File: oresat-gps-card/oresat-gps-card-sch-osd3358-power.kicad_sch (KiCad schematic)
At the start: 52 parts, among them Q6 MMBT2907, U1 OSD3358-512M-BSM, U10 SN74LVC1G07DCK, U13 RCLAMP0504FB, U14 TLVH431

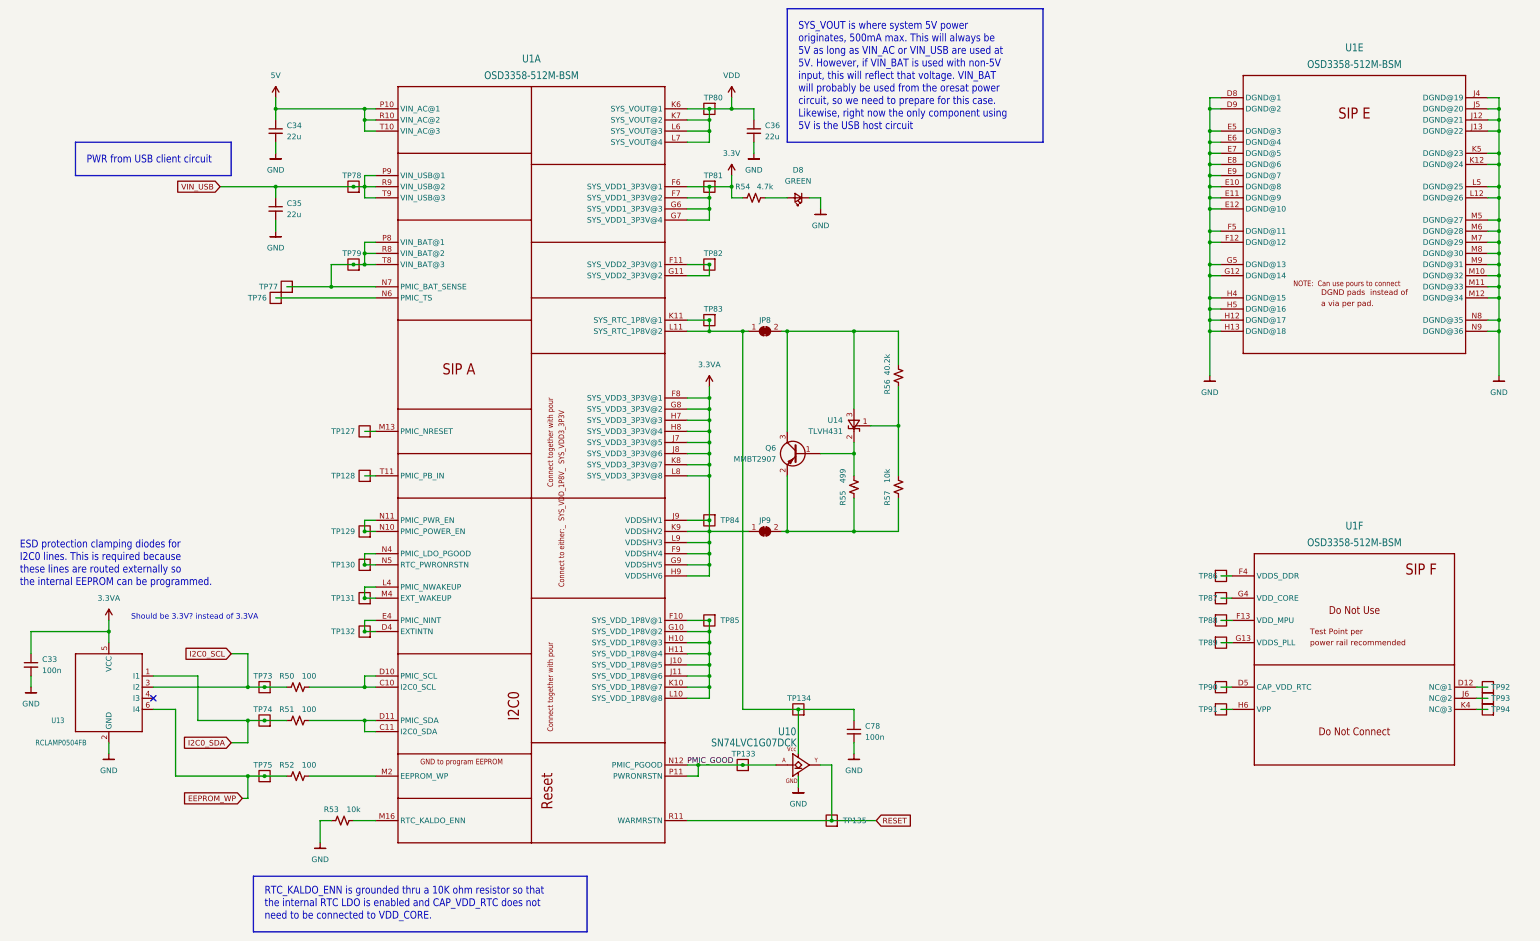
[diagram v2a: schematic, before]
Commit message: Updated GPS card with changes from C3 and notes. Fixed library issues
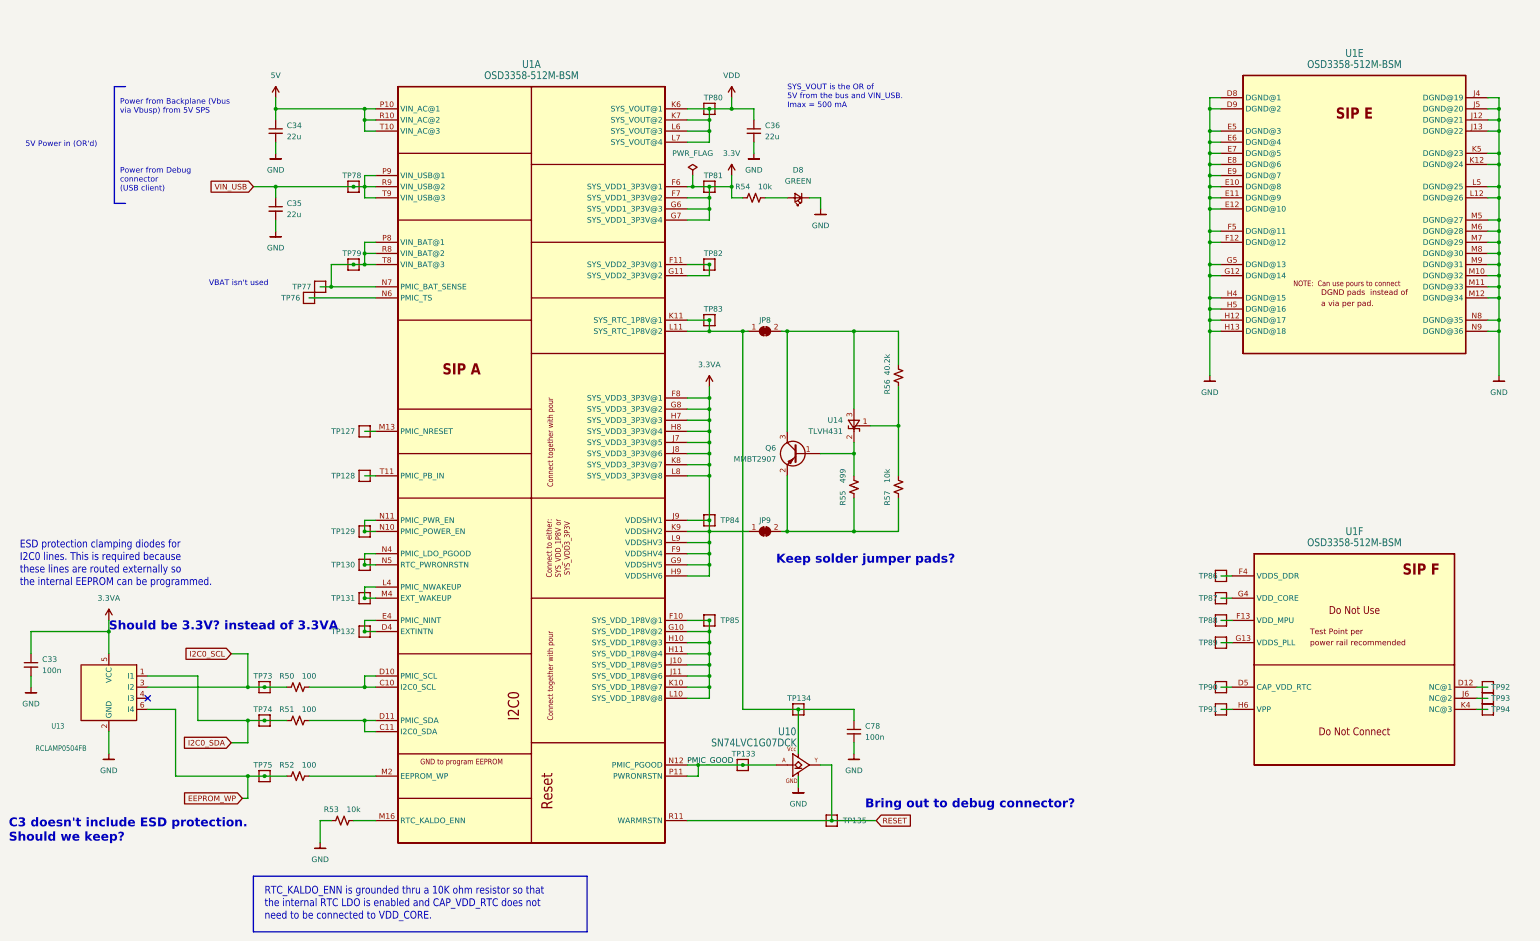
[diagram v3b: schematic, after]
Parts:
- R54: value 4.7k -> 10k
- TP127, TP128, TP129, TP130, TP131, TP132, TP133, TP134, TP135, TP73, TP74, TP75, TP76, TP77, TP78, TP79, TP80, TP81, TP82, TP83, TP84, TP85, TP86, TP87, TP88, TP89, TP90, TP91, TP92, TP93, TP94: value Test-Point -> 0.03x0.04; footprint OreSat-TestPoint:PAD.03X.04 -> oresat-misc:TestPoint_Pad_D1.0mm; symbol OreSat-TestPoint:Test-Point -> oresat-misc:Test-Point-1mm-round
- U1: footprint oresat-footprints:U-Octavo-OSD335X-BGA-256 -> oresat-ics:U-Octavo-OSD335X-BGA-256; symbol U-OSD3358-512M-BSM:OSD3358-512M-BSM -> oresat-ics:OSD3358-512M-BSM
- U10: symbol U-TI-SN74LVC1G07DCK:SN74LVC1G07DCK -> oresat-ics:SN74LVC1G07DCK
- U13: symbol U-Semtech-RCLAMP0504FB-tvs-diodes:RCLAMP0504FB -> oresat-ics:RCLAMP0504FB
- U14: footprint oresat-footprints:SOT23 -> Package_TO_SOT_SMD:SOT-23; symbol U-TI-TLVH431-shunt-regulator:TLVH431 -> oresat-ics:TLVH431
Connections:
- net VDD renamed 1.1V
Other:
- note added: "5V Power in (OR'd)"
- note added: "Bring out to debug connector?"
- note added: "C3 doesn't include ESD protection. Should we keep?"
- note added: "Keep solder jumper pads?"
- note added: "Power from Backplane (Vbus via Vbusp) from 5V SPS"
- note added: "Power from Debug connector (USB client)"
- note added: "SYS_VOUT is the OR of 5V from the bus and VIN_USB. Imax = 500 mA"
- note added: "VBAT isn't used"
- note removed: "PWR from USB client circuit"
- note removed: "SYS_VOUT is where system 5V power originates, 500mA max. This will always be 5V as long as VIN_AC or VIN_USB are used at 5V. However, if VIN_BAT is used with non-5V input, this will reflect that voltage. VIN_BAT will probably be used from the oresat power circuit, so we need to prepare for this case. Likewise, right now the only component using 5V is the USB host circuit"

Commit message: Updated GPS card
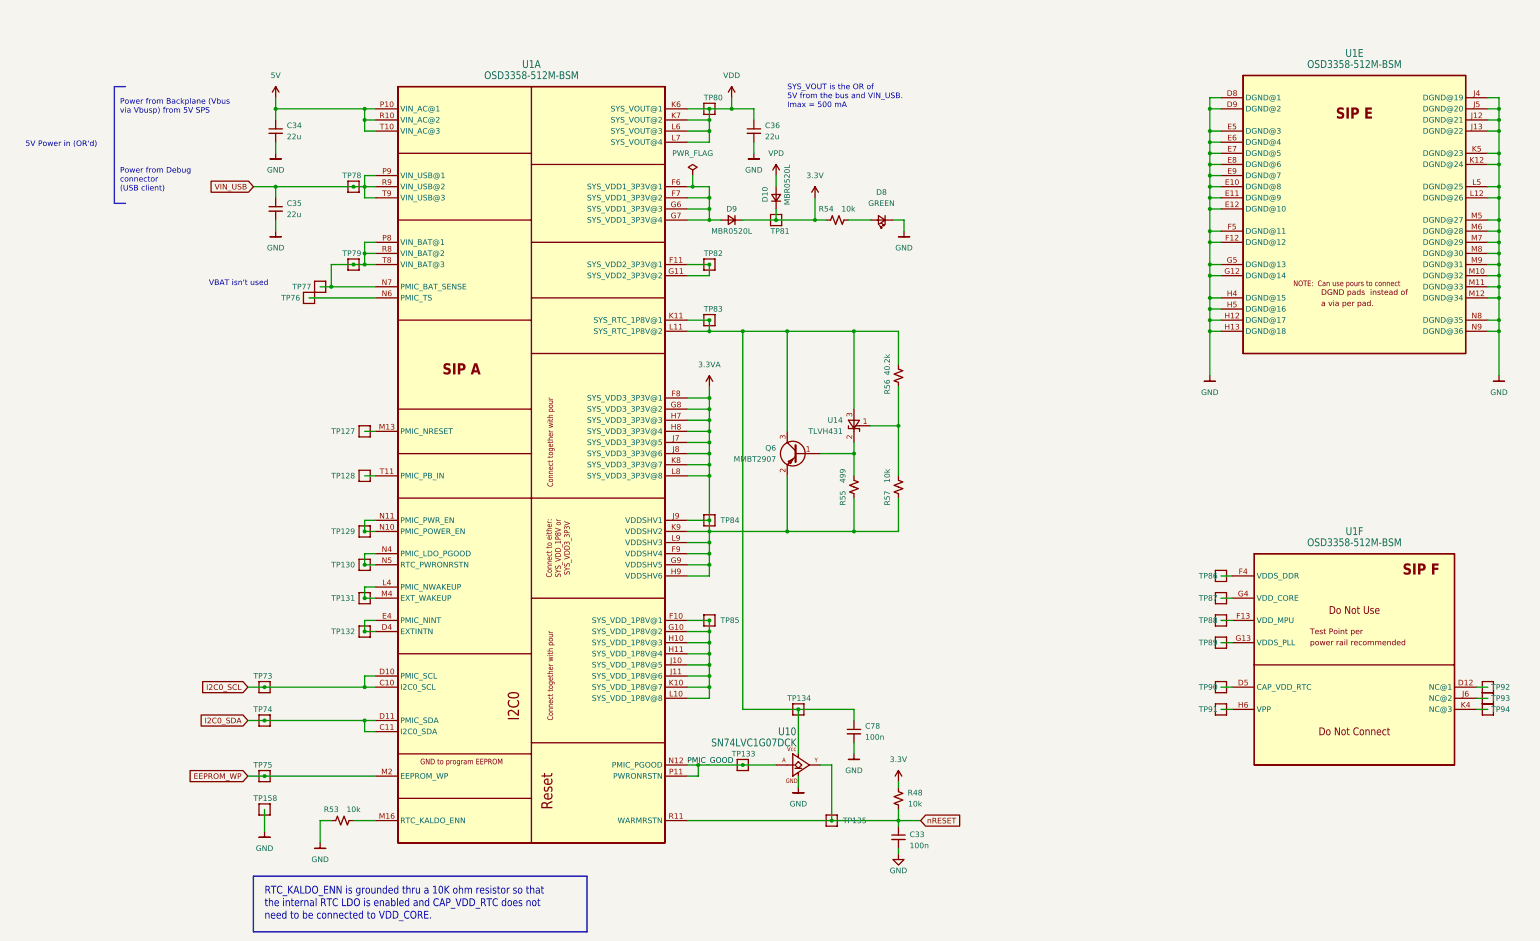
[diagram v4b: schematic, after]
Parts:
- removed JP8, JP9: SolderJumper_2_Bridged, oresat-footprints:SMT-JUMPER_2_NC_TRACE_SILK, symbol Jumper:SolderJumper_2_Bridged
- removed R50, R51, R52: 100, Resistor_SMD:R_0603_1608Metric, symbol Device:R_Small_US
- removed U13: RCLAMP0504FB, Package_TO_SOT_SMD:SOT-363_SC-70-6, symbol oresat-ics:RCLAMP0504FB
- added D10, D9: MBR0520L, Diode_SMD:D_SOD-123, symbol Device:D_Small
- added R48: 10k, Resistor_SMD:R_0603_1608Metric, symbol Device:R_Small_US
- added TP158: 0.03x0.04, oresat-misc:TestPoint-0.75mm-th, symbol oresat-misc:Test-Point-1mm-round
- TP73, TP74, TP75: footprint oresat-misc:TestPoint_Pad_D1.0mm -> oresat-misc:TestPoint-0.75mm-th
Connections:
- net 3.3V: now also D10.1 (K), D9.1 (K), R48.2; no longer U1.F6 (SYS_VDD1_3P3V@1), U1.F7 (SYS_VDD1_3P3V@2), U1.G6 (SYS_VDD1_3P3V@3), U1.G7 (SYS_VDD1_3P3V@4)
- net 3.3VA: now also Q6.2 (E), R55.1, R57.1; no longer C33.1
- net EEPROM_WP: now also U1.M2 (EEPROM_WP)
- net GND: now also TP158.1
- net I2C0_SCL: now also U1.C10 (I2C0_SCL), U1.D10 (PMIC_SCL)
- net I2C0_SDA: now also U1.C11 (I2C0_SDA), U1.D11 (PMIC_SDA)
- net at C78.1, TP134.1, TP83.1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: now also Q6.3 (C), R56.2, U14.3 (A)
- net RESET renamed nRESET
- net nRESET: now also C33.1, R48.1
- new net: D9.2 (A), U1.F6 (SYS_VDD1_3P3V@1), U1.F7 (SYS_VDD1_3P3V@2), U1.G6 (SYS_VDD1_3P3V@3), U1.G7 (SYS_VDD1_3P3V@4)
- new net VPD: D10.2 (A)
- no-connect marks 1 -> 0
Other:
- note removed: "Bring out to debug connector?"
- note removed: "C3 doesn't include ESD protection. Should we keep?"
- note removed: "ESD protection clamping diodes for I2C0 lines. This is required because these lines are routed externally so the internal EEPROM can be programmed."
- note removed: "Keep solder jumper pads?"
- note removed: "Should be 3.3V? instead of 3.3VA"
- moved on the sheet: D8, R54, TP81

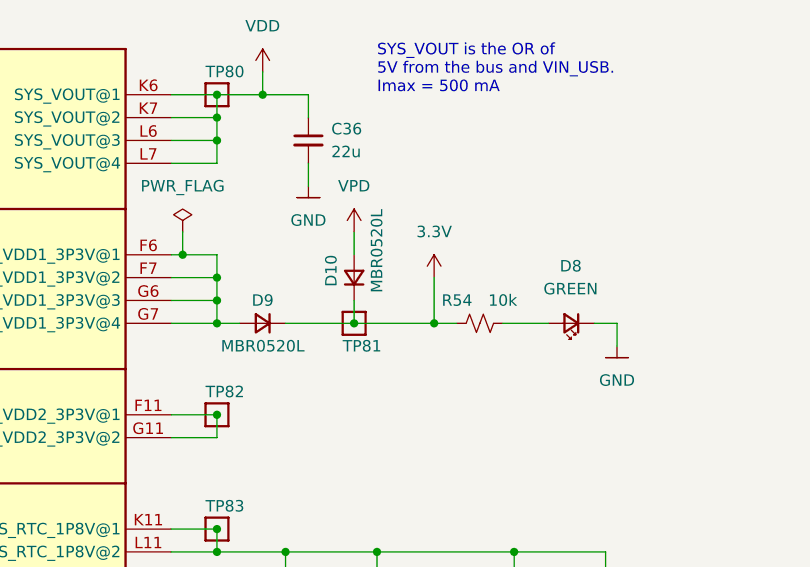
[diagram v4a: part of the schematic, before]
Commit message: Update RF path for sunstone board run, and connected VPD diodes
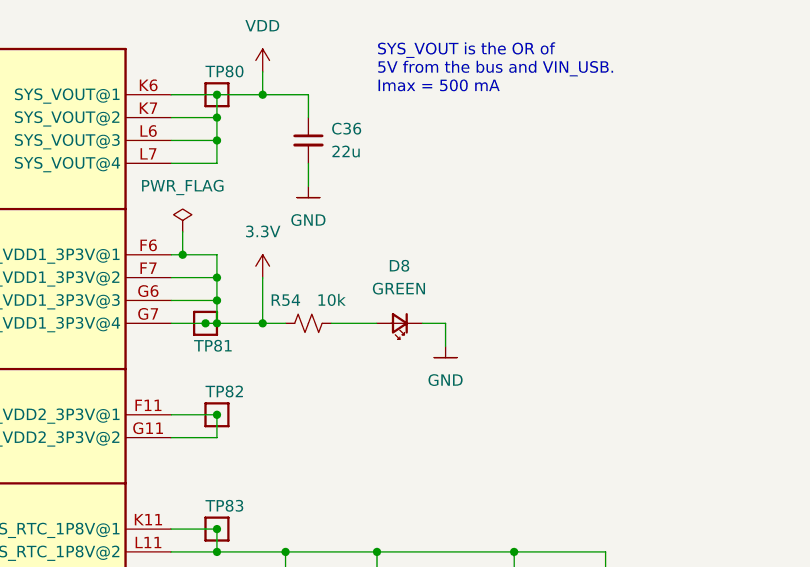
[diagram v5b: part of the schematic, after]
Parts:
- removed D10, D9: MBR0520L, Diode_SMD:D_SOD-123, symbol Device:D_Small
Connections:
- net 3.3V: now also U1.F6 (SYS_VDD1_3P3V@1), U1.F7 (SYS_VDD1_3P3V@2), U1.G6 (SYS_VDD1_3P3V@3), U1.G7 (SYS_VDD1_3P3V@4)
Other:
- moved on the sheet: D8, R54, TP81

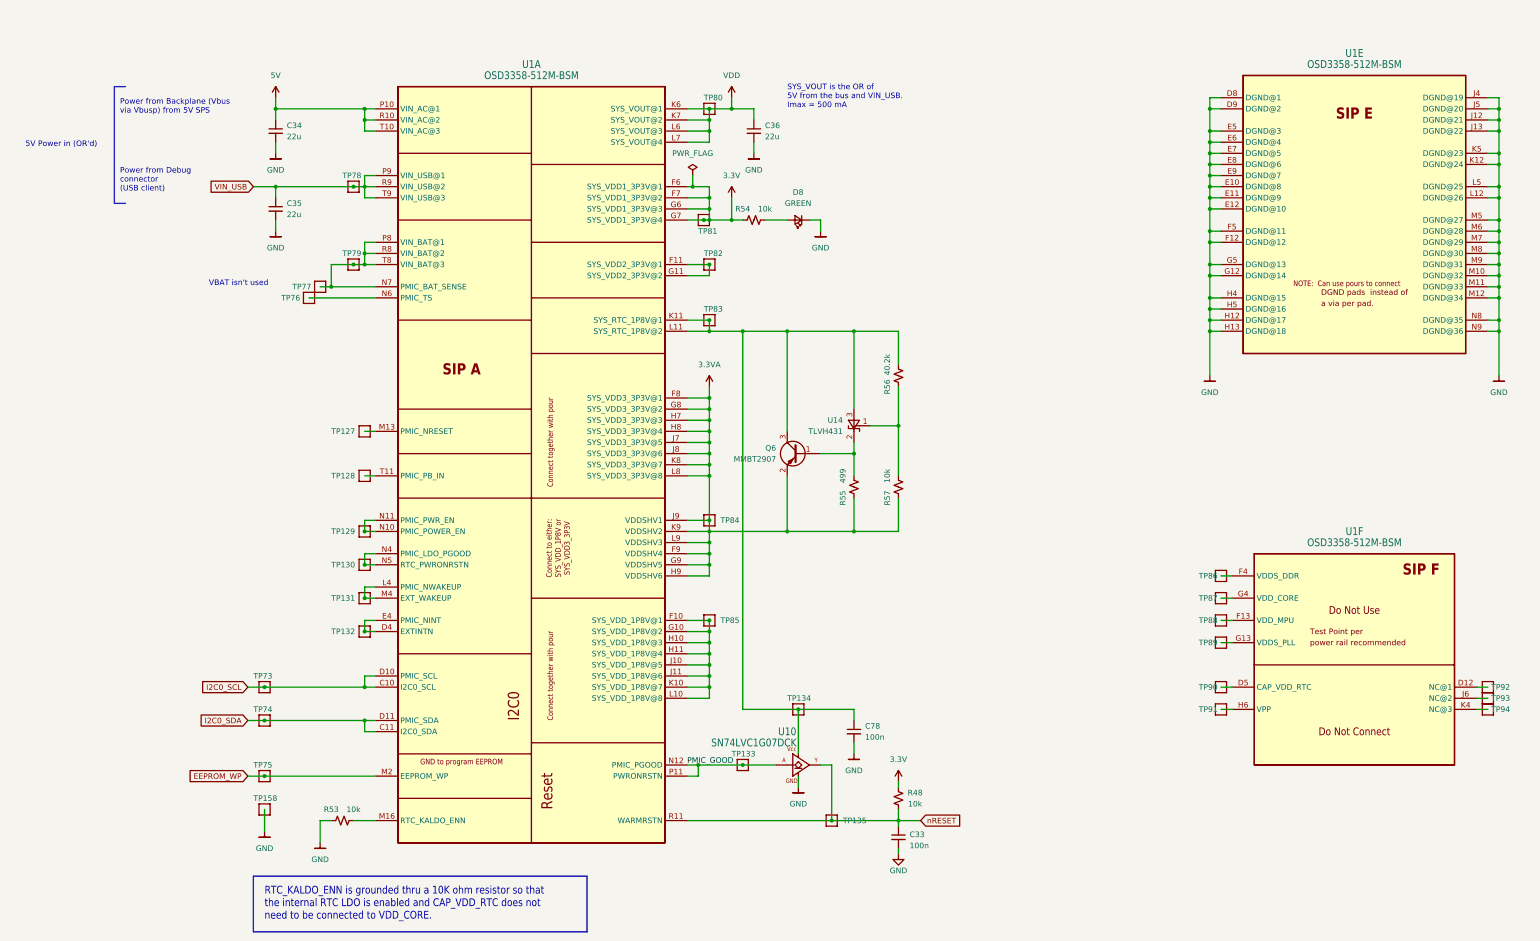
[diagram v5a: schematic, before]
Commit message: Cleaned up ERC and DRC errors on GPS card
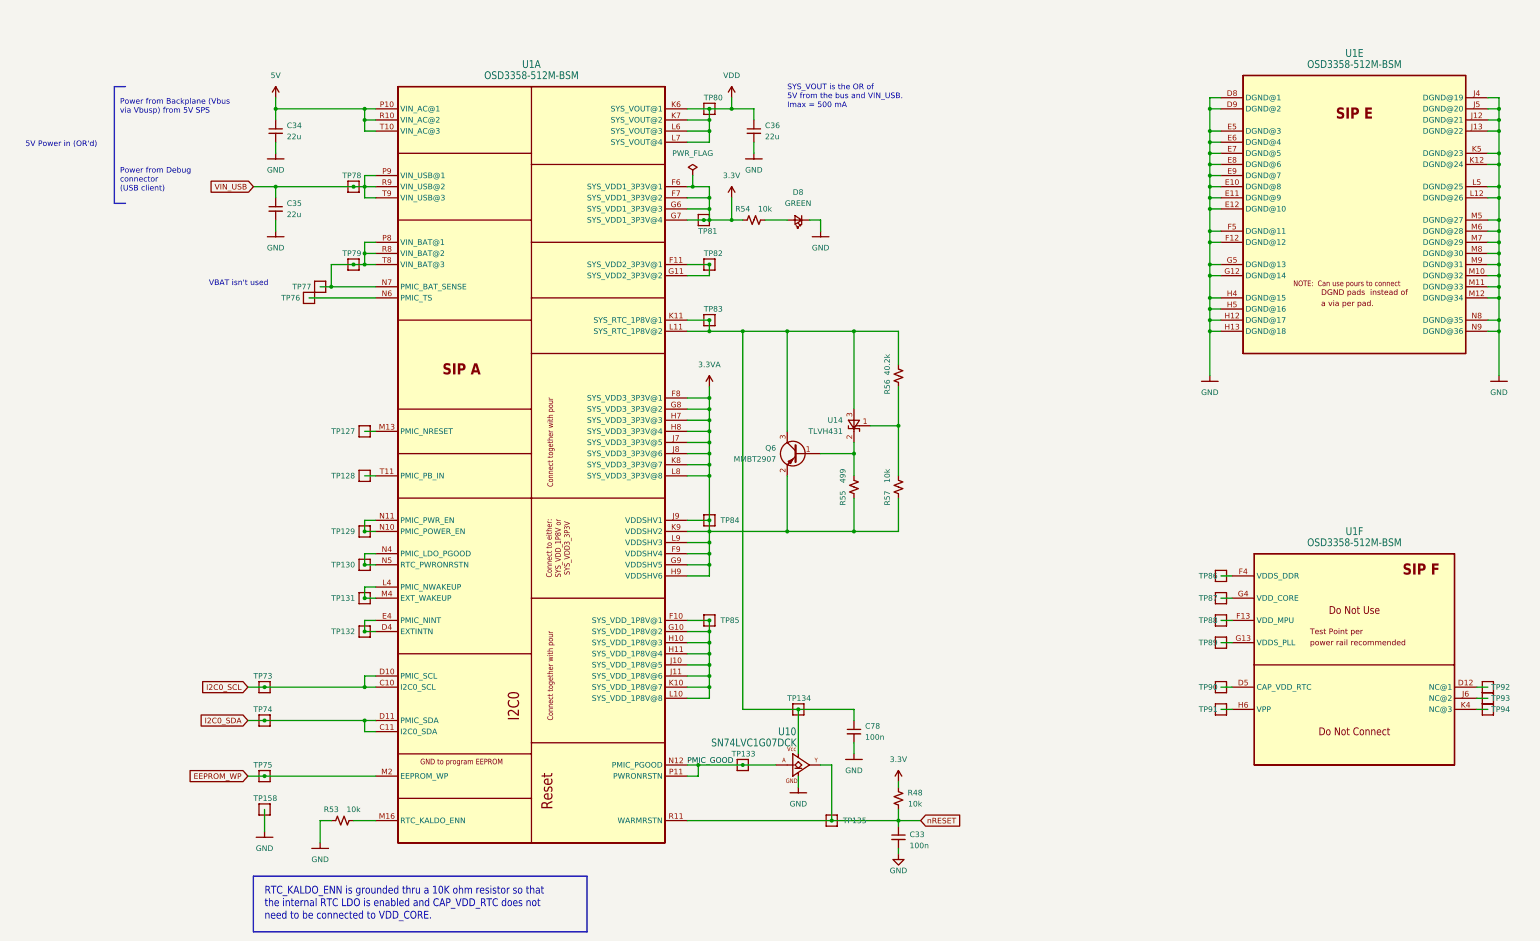
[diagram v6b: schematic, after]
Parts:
- Q6: footprint oresat-footprints:SOT23 -> oresat-ics:SOT23
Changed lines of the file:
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@@
       (effects (font (size 1.27 1.27)) (justify left))
     )
-    (property "Footprint" "oresat-footprints:SOT23" (at 190.5 129.54 0)
+    (property "Footprint" "oresat-ics:SOT23" (at 190.5 129.54 0)
       (effects (font (size 1.27 1.27)) hide)
     )

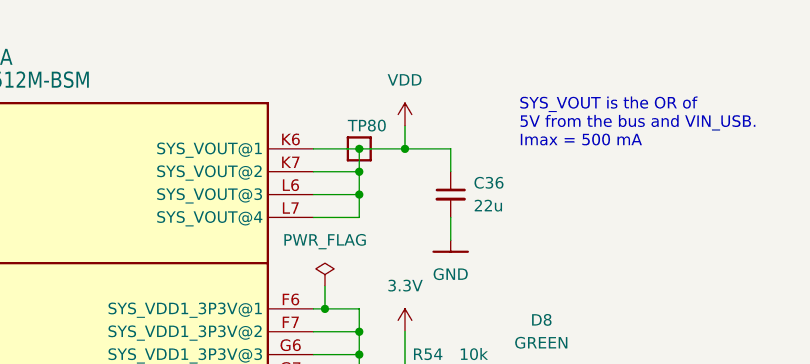
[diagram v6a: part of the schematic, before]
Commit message: Updated KiCAD 8, updated schematic sheet info, polished some schematic things, and made DNP parts DNP.
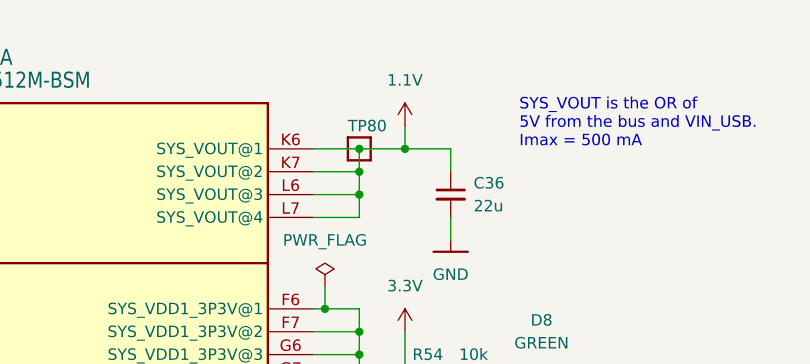
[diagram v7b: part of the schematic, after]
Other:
- title: (none) -> OreSat GPS Card
